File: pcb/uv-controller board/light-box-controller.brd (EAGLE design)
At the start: 100 x 60 mm, 31 parts, among them IC1 LDL112D33R, J1 12 VIN, J2 UVLED-OUT, Q1 FQP30N06L, U1 L7805, U2 ESP-WROOM-32

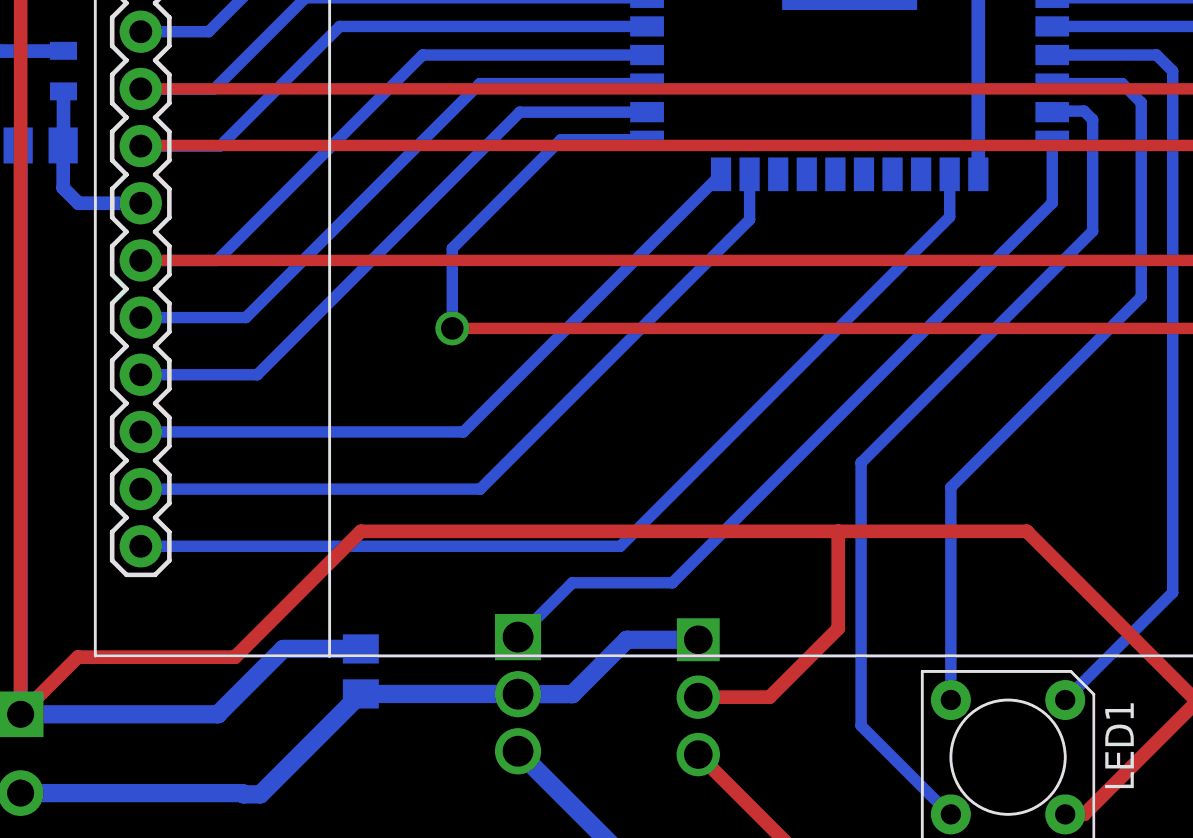
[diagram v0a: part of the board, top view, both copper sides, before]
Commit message: added pull down resisitor
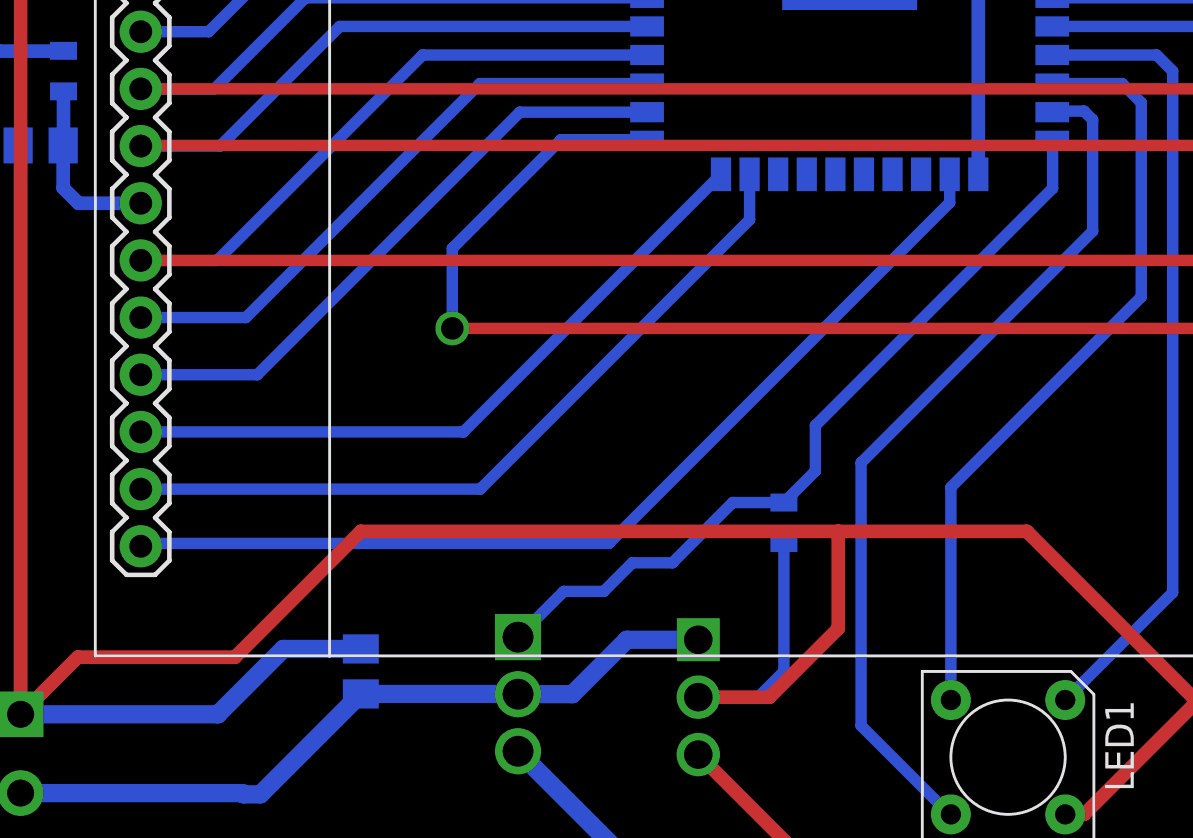
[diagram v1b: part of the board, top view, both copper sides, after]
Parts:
- added R5: 10 K, passives:0805
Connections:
- net GND: now also R5.2
- net UVLED_CONTROL: now also R5.1
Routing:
- net GND: track 515.3 -> 525.3 mm
- net UVLED_CONTROL: track 34.5 -> 35.3 mm
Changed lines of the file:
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@@
 </layers>
 <board>
-<fusionsync huburn="a.cGVyc29uYWw6dWUyZDRlMmZl" projecturn="a.cGVyc29uYWw6dWUyZDRlMmZlIzIwMjAwMzE3Mjc1NDUxMTgx" f3durn="urn:adsk.wipprod:dm.lineage:iAvUIwwFSgWR0kxmvv-Xbw" pcbguid="" lastpulledtime="" lastsyncedchangeguid="" latestrevisionid="efc455f2-aa56-41e5-8bb2-e23d9535d1e5" lastsyncedrevisionid="efc455f2-aa56-41e5-8bb2-e23d9535d1e5" lastboardhashguid="66f598d6-a76d-8933-e257-dcca98692c9d" lastpushedtime="2020-07-08T20:58:24Z" linktopcb3d="true"/>
+<fusionsync huburn="a.cGVyc29uYWw6dWUyZDRlMmZl" projecturn="a.cGVyc29uYWw6dWUyZDRlMmZlIzIwMjAwMzE3Mjc1NDUxMTgx" f3durn="urn:adsk.wipprod:dm.lineage:iAvUIwwFSgWR0kxmvv-Xbw" pcbguid="" lastpulledtime="" lastsyncedchangeguid="" latestrevisionid="efc455f2-aa56-41e5-8bb2-e23d9535d1e5" lastsyncedrevisionid="efc455f2-aa56-41e5-8bb2-e23d9535d1e5" lastboardhashguid="66f598d6-a76d-8933-e257-dcca98692c9d" lastpushedtime="2020-07-08T20:58:24Z" linktopcb3d="false"/>
 <plain>
 <wire x1="0" y1="0" x2="100" y2="0" width="0" layer="20"/>
@@
 <attribute name="VALUE" x="74.93" y="33.02" size="1.27" layer="27" rot="R90"/>
 </element>
+<element name="R5" library="passives" package="0805" value="10 K" x="37.592" y="16.764" smashed="yes" rot="MR270">
+<attribute name="NAME" x="36.7665" y="17.526" size="0.4064" layer="26" rot="MR270"/>
+<attribute name="VALUE" x="38.989" y="17.78" size="0.4064" layer="28" rot="MR270"/>
+</element>
 </elements>
 <signals>
@@
 <wire x1="12.446" y1="8.255" x2="3.683" y2="8.255" width="0.8128" layer="16"/>
 <wire x1="15.351" y1="11.16" x2="12.446" y2="8.255" width="0.8128" layer="16"/>
+<contactref element="R5" pad="2"/>
+<wire x1="33.788" y1="9.017" x2="36.449" y2="9.017" width="0.508" layer="16"/>
+<wire x1="37.592" y1="10.16" x2="37.592" y2="15.864" width="0.508" layer="16"/>
+<wire x1="36.449" y1="9.017" x2="37.592" y2="10.16" width="0.508" layer="16"/>
 </signal>
 <signal name="UVLED_CONTROL">
 <contactref element="Q1" pad="1"/>
 <contactref element="U2" pad="14"/>
-<wire x1="25.781" y1="11.684" x2="28.194" y2="14.097" width="0.508" layer="16"/>
-<wire x1="28.194" y1="14.097" x2="32.639" y2="14.097" width="0.508" layer="16"/>
-<wire x1="32.639" y1="14.097" x2="49.513" y2="30.971" width="0.508" layer="16"/>
-<wire x1="49.513" y1="30.971" x2="49.513" y2="33.735" width="0.508" layer="16"/>
+<contactref element="R5" pad="1"/>
+<wire x1="25.781" y1="11.684" x2="27.813" y2="13.716" width="0.508" layer="16"/>
+<wire x1="27.813" y1="13.716" x2="29.591" y2="13.716" width="0.508" layer="16"/>
+<wire x1="29.591" y1="13.716" x2="30.861" y2="14.986" width="0.508" layer="16"/>
+<wire x1="30.861" y1="14.986" x2="32.639" y2="14.986" width="0.508" layer="16"/>
+<wire x1="35.317" y1="17.664" x2="37.592" y2="17.664" width="0.508" layer="16"/>
+<wire x1="32.639" y1="14.986" x2="35.317" y2="17.664" width="0.508" layer="16"/>
+<wire x1="37.592" y1="17.664" x2="38.989" y2="19.061" width="0.508" layer="16"/>
+<wire x1="38.989" y1="21.082" x2="49.53" y2="31.623" width="0.508" layer="16"/>
+<wire x1="49.53" y1="31.623" x2="49.53" y2="33.718" width="0.508" layer="16"/>
+<wire x1="49.53" y1="33.718" x2="49.513" y2="33.735" width="0.508" layer="16"/>
+<wire x1="38.989" y1="19.061" x2="38.989" y2="21.082" width="0.508" layer="16"/>
 </signal>
 <signal name="N$12">
@@
 <contactref element="U$2" pad="14"/>
 <contactref element="U2" pad="16"/>
-<wire x1="44.958" y1="32.245" x2="44.958" y2="30.353" width="0.508" layer="16"/>
-<wire x1="30.325" y1="15.72" x2="9.02" y2="15.72" width="0.508" layer="16"/>
-<wire x1="44.958" y1="30.353" x2="30.325" y2="15.72" width="0.508" layer="16"/>
+<wire x1="44.958" y1="32.245" x2="44.958" y2="30.988" width="0.508" layer="16"/>
+<wire x1="29.817" y1="15.847" x2="9.147" y2="15.847" width="0.508" layer="16"/>
+<wire x1="9.147" y1="15.847" x2="9.02" y2="15.72" width="0.508" layer="16"/>
+<wire x1="44.958" y1="30.988" x2="29.817" y2="15.847" width="0.508" layer="16"/>
 </signal>
 <signal name="SD_CS">

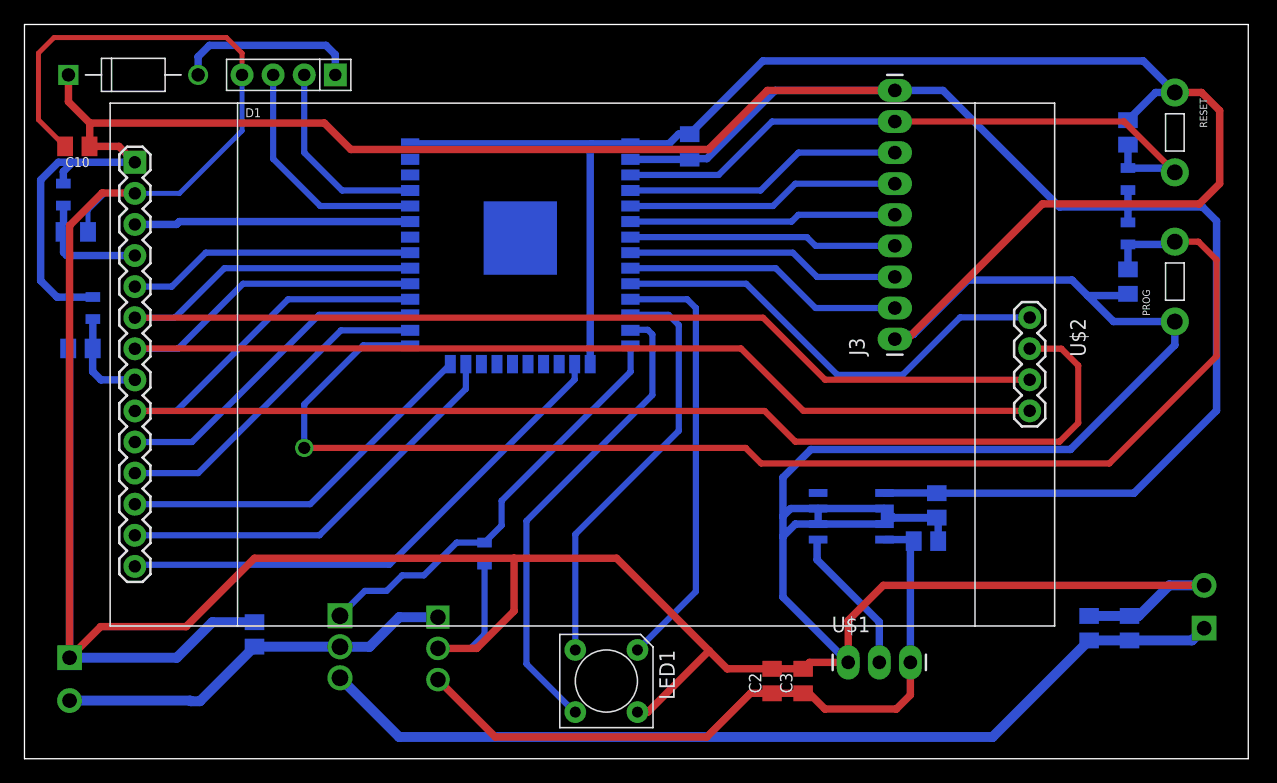
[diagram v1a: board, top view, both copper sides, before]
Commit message: update to use ground planes
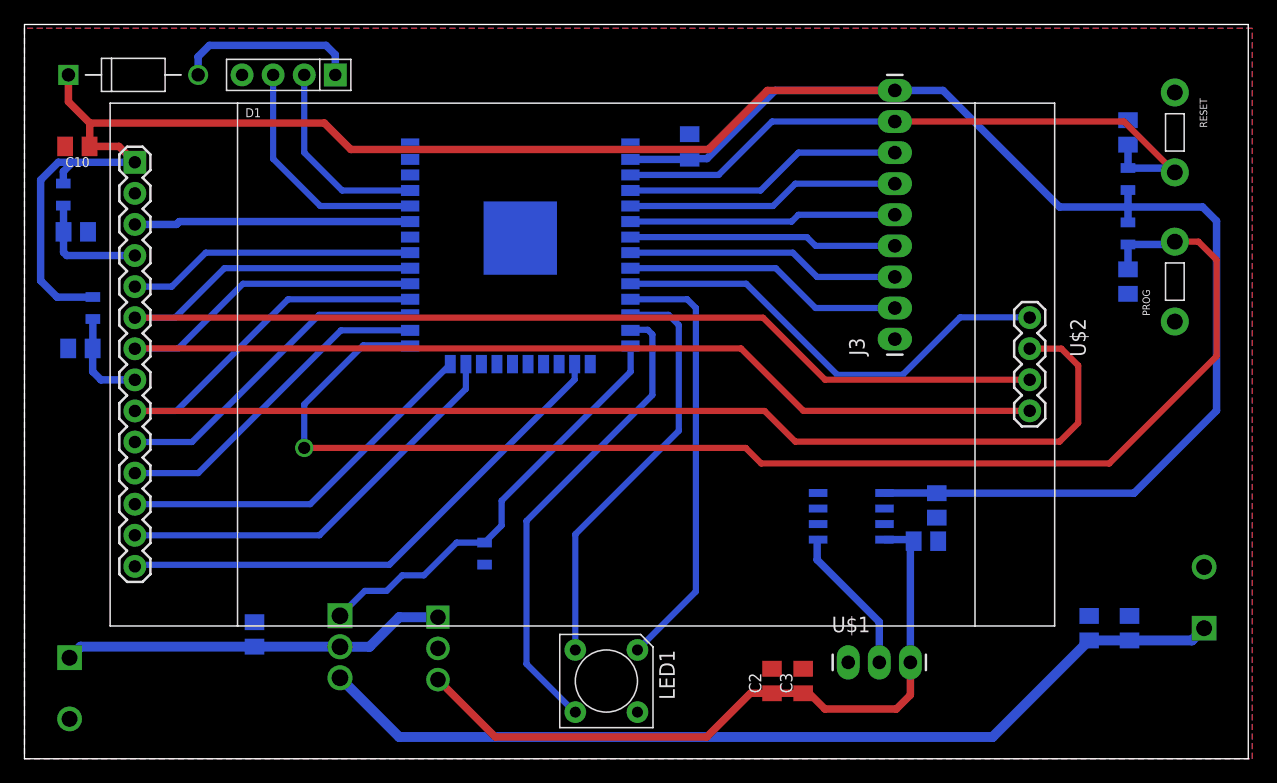
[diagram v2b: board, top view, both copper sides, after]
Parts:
- J1, J2: device connector:SCREWTERMINAL-3.5MM-2 -> connector:SCREWTERMINAL-5MM-2
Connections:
- net GND: now also J1.2; no longer J1.1
- net V12: now also J1.1; no longer J1.2
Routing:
- net GND: track 525.3 -> 0.00 mm
- net V12: track 33.0 -> 31.5 mm
- added copper zone on layer 1, net GND
- added copper zone on layer 16, net GND

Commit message: moving away from IO15 as I'm pretty sure its messing up the touch screen
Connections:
- net TOUCH_DATA_OUT: now also U2.36; no longer U2.23
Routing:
- net TOUCH_DATA_OUT: track 34.0 -> 48.5 mm, vias 0 -> 1
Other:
- board text added: "11282020:v3"
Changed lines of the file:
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@@
 <wire x1="100" y1="60" x2="0" y2="60" width="0" layer="20"/>
 <wire x1="0" y1="60" x2="0" y2="0" width="0" layer="20"/>
+<text x="96.52" y="2.54" size="1.27" layer="26" rot="MR0">11282020:v3</text>
 </plain>
 <attributes>
@@
 <signal name="TOUCH_DATA_OUT">
 <contactref element="U$2" pad="13"/>
-<contactref element="U2" pad="23"/>
-<wire x1="36.068" y1="32.245" x2="36.068" y2="30.226" width="0.508" layer="16"/>
-<wire x1="36.068" y1="30.226" x2="24.102" y2="18.26" width="0.508" layer="16"/>
-<wire x1="24.102" y1="18.26" x2="9.02" y2="18.26" width="0.508" layer="16"/>
+<contactref element="U2" pad="36"/>
+<wire x1="9.02" y1="18.26" x2="14.704" y2="18.26" width="0.508" layer="1"/>
+<wire x1="14.704" y1="18.26" x2="19.177" y2="22.733" width="0.508" layer="1"/>
+<via x="19.177" y="22.733" extent="1-16" drill="0.8"/>
+<wire x1="22.86" y1="22.733" x2="35.052" y2="34.925" width="0.508" layer="16"/>
+<wire x1="35.052" y1="34.925" x2="35.052" y2="46.355" width="0.508" layer="16"/>
+<wire x1="35.052" y1="46.355" x2="33.655" y2="47.752" width="0.508" layer="16"/>
+<wire x1="33.655" y1="47.752" x2="31.56" y2="47.752" width="0.508" layer="16"/>
+<wire x1="31.56" y1="47.752" x2="31.513" y2="47.705" width="0.508" layer="16"/>
+<wire x1="19.177" y1="22.733" x2="22.86" y2="22.733" width="0.508" layer="16"/>
 </signal>
 <signal name="TOUCH_IRQ">

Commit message: added notes to ensure I don't mess up the n-channel mosfet again.  :)
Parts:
- added U$4: CMD_C0DE_LOGOCMD_CODE_LOGO_SILK, logos:CMD_C0DE_LOGO_SILK
- moved C1 9.06 mm to (9.78, 9.27)
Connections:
- removed net N$12: C5.1, C6.1, J2.1, Q1.3
- new net N$2: J2.2, Q1.2
- net GND: now also Q1.3; no longer J2.2
- net V12: now also C5.1, C6.1, J2.1; no longer Q1.2
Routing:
- net V12: track 31.5 -> 112.3 mm
- net N$12: track 76.3 -> 0.00 mm
- net N$2: track 0.00 -> 75.7 mm
- net V5: track 58.2 -> 55.2 mm
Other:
- board text added: "05172021:v4"
- board text removed: "11282020:v3"

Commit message: adding docs and added voltage multipler for mosfet gate
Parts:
- added C14: 1.6 nF, passives:C0805K
- added C15: 1 uF, passives:C0805K
- added C16, C17: 10 uF, passives:C0805K
- added C18: 0.1 uF, passives:C0805K
- added D2: DIODE-SCHOTTKYSOD-123FL, passives:SOD-123FL
- added IC2: TPS61085DGKR, dc-converters:SOP65P490X110-8N
- added L1: CDPH4D19FNP-3R3MC, passives:CDPH4D19FNP3R3MC
- added R6: 47 K, passives:0805
- added R7: 158 K, passives:0805
- added R8: 18.2 K, passives:0805
- added U$5, U$6: FIDUCIAL, logos:FIDUCIAL_1MM
- moved R5 8.89 mm to (28.7, 16.8)
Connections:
- new net FB: IC2.2, R7.2, R8.1
- new net N$3: IC2.1, R6.2
- new net N$5: C14.1, R6.1
- new net N$8: C18.1, IC2.8
- new net UVLED_BEFORE_DIODE: D2.A, IC2.5, L1.1
- new net UVLED_CONTROL_EN: IC2.3, U2.14
- net GND: now also C14.2, C15.2, C16.2, C17.2, C18.2, IC2.4, R8.2
- net UVLED_CONTROL: now also C16.1, C17.1, D2.C, R7.1; no longer U2.14
- net V3.3: now also C15.1, IC2.6, IC2.7, L1.2
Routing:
- net V3.3: track 205.6 -> 283.7 mm
- net UVLED_BEFORE_DIODE: track 0.00 -> 20.7 mm
- net UVLED_CONTROL: track 35.3 -> 50.8 mm
- net UVLED_CONTROL_EN: track 0.00 -> 11.9 mm
- net FB: track 0.00 -> 5.41 mm
- net RED: track 34.3 -> 37.7 mm
- net BLUE: track 35.6 -> 38.1 mm
- net N$5: track 0.00 -> 1.80 mm
- net N$8: track 0.00 -> 1.72 mm
- net GREEN: track 38.8 -> 40.5 mm
- net N$3: track 0.00 -> 1.44 mm
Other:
- board text added: "07232021:v5"
- board text removed: "05172021:v4"
